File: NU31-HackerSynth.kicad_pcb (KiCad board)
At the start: 2 copper layers, 180 x 110 mm, 137 parts, among them J1 Conn_02x09_Odd_Even, J2 GREEN, J3 Barrel_Jack, J4 AudioJack2_SwitchT, J5 AudioJack2_SwitchT, J6 AudioJack2_SwitchT, J7 Eurorack Power, Q1 BC547, Q2 BC547, Q3 BC547, Q4 BC547, SW1 SW_DPDT, SW2 SW_SPDT, SW3 SW_Rotary_1x8_MP, U1 LM358, U2 LM358, U3 LM358, U4 CD4017, U5 LM358, U6 LM358, U7 LM358

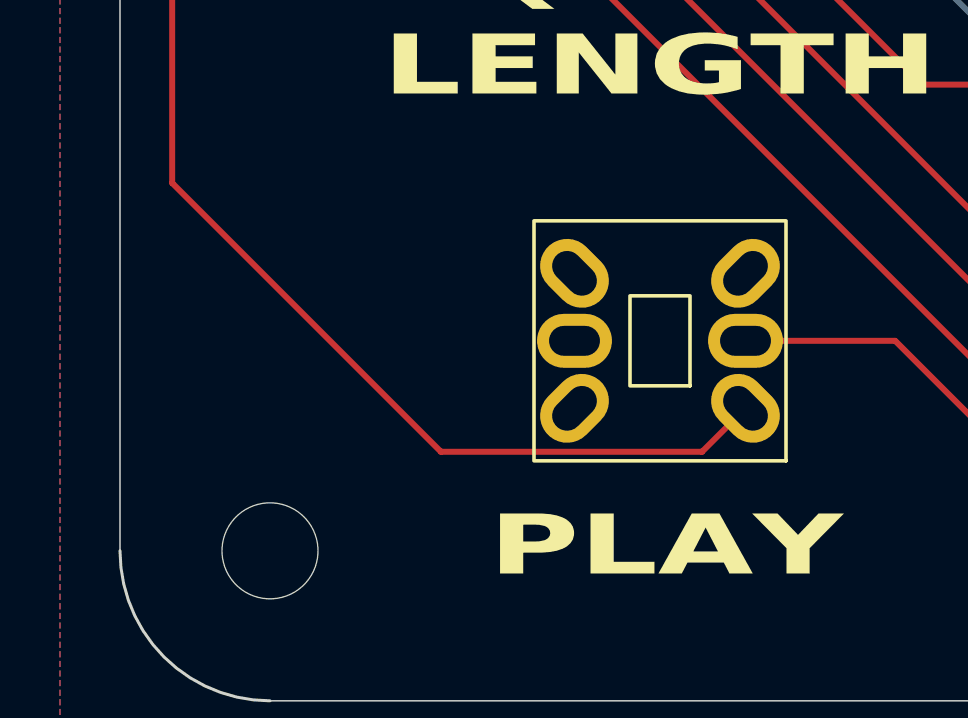
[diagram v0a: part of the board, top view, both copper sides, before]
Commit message: fixed clock switch pinout and footprint
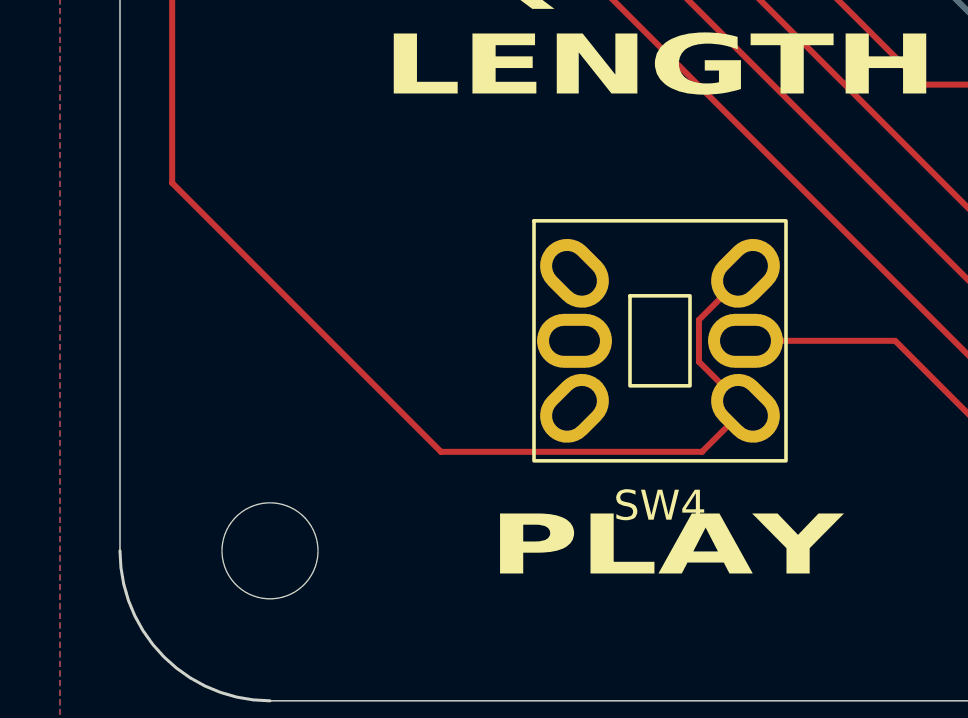
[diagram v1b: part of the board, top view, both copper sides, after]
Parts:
- removed SW2: SW_SPDT, SpaceCow:8x8_DPDT_Push_Button
- added SW4: SW_DPST, SpaceCow:8x8_DPDT_Push_Button, F.Cu at (68.0, 148.0)
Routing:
- net /SEQ_CLOCK_IN: track 223.2 -> 229.0 mm
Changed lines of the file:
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@@
 		)
 	)
+	(footprint "SpaceCow:8x8_DPDT_Push_Button"
+		(layer "F.Cu")
+		(at 68 148)
+		(property "Reference" "SW4"
+			(at 0 5.5 0)
+			(unlocked yes)
+			(layer "F.SilkS")
+			(effects
+				(font
+					(size 1 1)
+					(thickness 0.15)
+				)
+			)
+		)
+		(property "Value" "SW_DPST"
+			(at 0 7 0)
+			(unlocked yes)
+			(layer "F.Fab")
+			(effects
+				(font
+					(size 1 1)
+					(thickness 0.15)
+				)
+			)
+		)
+		(property "Datasheet" "~"
+			(at 0 0 0)
+			(unlocked yes)
+			(layer "F.Fab")
+			(hide yes)
+			(effects
+				(font
+					(size 1 1)
+					(thickness 0.15)
+				)
+			)
+		)
+		(property "Description" "Double Pole Single Throw (DPST) Switch"
+			(at 0 0 0)
+			(unlocked yes)
+			(layer "F.Fab")
+			(hide yes)
+			(effects
+				(font
+					(size 1 1)
+					(thickness 0.15)
+				)
+			)
+		)
+		(sheetname "/")
+		(sheetfile "NU31-HackerSynth.kicad_sch")
+		(attr through_hole)
+		(fp_rect
+			(start -4.2 -4)
+			(end 4.2 4)
+			(stroke
+				(width 0.12)
+				(type default)
+			)
+			(fill no)
+			(layer "F.SilkS")
+		)
+		(fp_rect
+			(start -1 -1.5)
+			(end 1 1.5)
+			(stroke
+				(width 0.12)
+				(type default)
+			)
+			(fill no)
+			(layer "F.SilkS")
+		)
+		(fp_rect
+			(start -4.4 -4.2)
+			(end 4.4 4.2)
+			(stroke
+				(width 0.05)
+				(type default)
+			)
+			(fill no)
+			(layer "F.CrtYd")
+		)
+		(fp_text user "${REFERENCE}"
+			(at -0.2 9.1 0)
+			(unlocked yes)
+			(layer "F.Fab")
+			(effects
+				(font
+					(size 1 1)
+					(thickness 0.15)
+				)
+			)
+		)
+		(pad "1" thru_hole oval
+			(at -2.85 -2.25 315)
+			(size 2.5 1.8)
+			(drill oval 1.7 1)
+			(layers "*.Cu" "*.Mask")
+			(remove_unused_layers no)
+			(net 1 "GND")
+			(pinfunction "1")
+			(pintype "passive")
+		)
+		(pad "1" thru_hole oval
+			(at -2.85 2.25 225)
+			(size 2.5 1.8)
+			(drill oval 1.7 1)
+			(layers "*.Cu" "*.Mask")
+			(remove_unused_layers no)
+			(net 1 "GND")
+			(pinfunction "1")
+			(pintype "passive")
+		)
+		(pad "2" thru_hole oval
+			(at -2.85 0 180)
+			(size 2.5 1.8)
+			(drill oval 1.7 1)
+			(layers "*.Cu" "*.Mask")
+			(remove_unused_layers no)
+			(net 1 "GND")
+			(pinfunction "2")
+			(pintype "passive")
+		)
+		(pad "3" thru_hole oval
+			(at 2.85 -2.25 225)
+			(size 2.5 1.8)
+			(drill oval 1.7 1)
+			(layers "*.Cu" "*.Mask")
+			(remove_unused_layers no)
+			(net 45 "/SEQ_CLOCK_IN")
+			(pinfunction "3")
+			(pintype "passive")
+		)
+		(pad "3" thru_hole oval
+			(at 2.85 2.25 135)
+			(size 2.5 1.8)
+			(drill oval 1.7 1)
+			(layers "*.Cu" "*.Mask")
+			(remove_unused_layers no)
+			(net 45 "/SEQ_CLOCK_IN")
+			(pinfunction "3")
+			(pintype "passive")
+		)
+		(pad "4" thru_hole oval
+			(at 2.85 0 180)
+			(size 2.5 1.8)
+			(drill oval 1.7 1)
+			(layers "*.Cu" "*.Mask")
+			(remove_unused_layers no)
+			(net 99 "Net-(R59-Pad2)")
+			(pinfunction "4")
+			(pintype "passive")
+		)
+		(embedded_fonts no)
+	)
 	(footprint "Resistor_THT:R_Axial_DIN0207_L6.3mm_D2.5mm_P10.16mm_Horizontal"
 		(layer "F.Cu")
@@
 		(embedded_fonts no)
 	)
-	(footprint "SpaceCow:8x8_DPDT_Push_Button"
-		(locked yes)
-		(layer "F.Cu")
-		(at 68 148 180)
-		(property "Reference" "SW2"
-			(at 0 -3 180)
-			(unlocked yes)
-			(layer "F.SilkS")
-			(hide yes)
-			(effects
-				(font
-					(size 0.8 0.8)
-					(thickness 0.16)
-					(bold yes)
-				)
-			)
-		)
-		(property "Value" "SW_SPDT"
-			(at 0 0 180)
-			(unlocked yes)
-			(layer "F.SilkS")
-			(hide yes)
-			(effects
-				(font
-					(size 0.8 0.65)
-					(thickness 0.15)
-					(italic yes)
-				)
-			)
-		)
-		(property "Datasheet" "~"
-			(at 0 0 180)
-			(unlocked yes)
-			(layer "F.Fab")
-			(hide yes)
-			(effects
-				(font
-					(size 1 1)
-					(thickness 0.15)
-				)
-			)
-		)
-		(property "Description" "Slide Switch, dual pole double throw"
-			(at 0 0 180)
-			(unlocked yes)
-			(layer "F.Fab")
-			(hide yes)
-			(effects
-				(font
-					(size 1 1)
-					(thickness 0.15)
-				)
-			)
-		)
-		(sheetname "/")
-		(sheetfile "NU31-HackerSynth.kicad_sch")
-		(attr through_hole)
-		(fp_rect
-			(start -1 -1.5)
-			(end 1 1.5)
-			(stroke
-				(width 0.12)
-				(type default)
-			)
-			(fill no)
-			(layer "F.SilkS")
-		)
-		(fp_rect
-			(start -4.2 -4)
-			(end 4.2 4)
-			(stroke
-				(width 0.12)
-				(type default)
-			)
-			(fill no)
-			(layer "F.SilkS")
-		)
-		(fp_rect
-			(start -4.4 -4.2)
-			(end 4.4 4.2)
-			(stroke
-				(width 0.05)
-				(type default)
-			)
-			(fill no)
-			(layer "F.CrtYd")
-		)
-		(fp_text user "${REFERENCE}"
-			(at -0.2 9.1 180)
-			(unlocked yes)
-			(layer "F.Fab")
-			(effects
-				(font
-					(size 0.8 0.8)
-					(thickness 0.16)
-					(bold yes)
-				)
-			)
-		)
-		(pad "1" thru_hole oval
-			(at -2.85 -2.25 135)
-			(size 2.5 1.8)
-			(drill oval 1.7 1)
-			(layers "*.Cu" "*.Mask")
-			(remove_unused_layers no)
-			(net 45 "/SEQ_CLOCK_IN")
-			(pinfunction "A")
-			(pintype "passive")
-		)
-		(pad "2" thru_hole oval
-			(at -2.85 0)
-			(size 2.5 1.8)
-			(drill oval 1.7 1)
-			(layers "*.Cu" "*.Mask")
-			(remove_unused_layers no)
-			(net 99 "Net-(R59-Pad2)")
-			(pinfunction "B")
-			(pintype "passive")
-		)
-		(pad "3" thru_hole oval
-			(at -2.85 2.25 45)
-			(size 2.5 1.8)
-			(drill oval 1.7 1)
-			(layers "*.Cu" "*.Mask")
-			(remove_unused_layers no)
-			(net 1 "GND")
-			(pinfunction "C")
-			(pintype "passive")
-		)
-		(pad "4" thru_hole oval
-			(at 2.85 -2.25 45)
-			(size 2.5 1.8)
-			(drill oval 1.7 1)
-			(layers "*.Cu" "*.Mask")
-			(remove_unused_layers no)
-			(net 1 "GND")
-			(pinfunction "A")
-			(pintype "passive")
-		)
-		(pad "5" thru_hole oval
-			(at 2.85 0)
-			(size 2.5 1.8)
-			(drill oval 1.7 1)
-			(layers "*.Cu" "*.Mask")
-			(remove_unused_layers no)
-			(net 1 "GND")
-			(pinfunction "B")
-			(pintype "passive")
-		)
-		(pad "6" thru_hole oval
-			(at 2.85 2.25 315)
-			(size 2.5 1.8)
-			(drill oval 1.7 1)
-			(layers "*.Cu" "*.Mask")
-			(remove_unused_layers no)
-			(net 1 "GND")
-			(pinfunction "C")
-			(pintype "passive")
-		)
-		(embedded_fonts no)
-	)
 	(footprint "Capacitor_THT:C_Disc_D5.1mm_W3.2mm_P5.00mm"
 		(layer "F.Cu")
@@
 	)
 	(segment
-		(start 148.64026 53)
-		(end 151.3 55.65974)
+		(start 69.299 147.301)
+		(end 69.299 148.699)
 		(width 0.2)
 		(layer "F.Cu")
@@
 	)
 	(segment
-		(start 60.698486 151.698486)
-		(end 51.739 142.739)
+		(start 151.3 71.4925)
+		(end 149.5125 73.28)
 		(width 0.2)
 		(layer "F.Cu")
@@
 	)
 	(segment
-		(start 69.401514 151.698486)
-		(end 60.698486 151.698486)
+		(start 60.7 151.7)
+		(end 51.739 142.739)
 		(width 0.2)
 		(layer "F.Cu")
@@
 	)
 	(segment
-		(start 151.3 55.65974)
-		(end 151.3 71.4925)
+		(start 148.64026 53)
+		(end 151.3 55.65974)
 		(width 0.2)
 		(layer "F.Cu")
@@
 	)
 	(segment
-		(start 151.3 71.4925)
-		(end 149.5125 73.28)
+		(start 69.4 151.7)
+		(end 60.7 151.7)
 		(width 0.2)
 		(layer "F.Cu")
@@
 	)
 	(segment
-		(start 51.739 142.739)
-		(end 51.739 68.361)
+		(start 69.299 148.699)
+		(end 70.85 150.25)
 		(width 0.2)
 		(layer "F.Cu")
@@
 	)
 	(segment
+		(start 51.739 142.739)
+		(end 51.739 68.361)
+		(width 0.2)
+		(layer "F.Cu")
+		(net 45)
+	)
+	(segment
+		(start 70.85 145.75)
+		(end 69.299 147.301)
+		(width 0.2)
+		(layer "F.Cu")
+		(net 45)
+	)
+	(segment
+		(start 151.3 55.65974)
+		(end 151.3 71.4925)
+		(width 0.2)
+		(layer "F.Cu")
+		(net 45)
+	)
+	(segment
 		(start 70.85 150.25)
-		(end 69.401514 151.698486)
+		(end 69.4 151.7)
 		(width 0.2)
 		(layer "F.Cu")

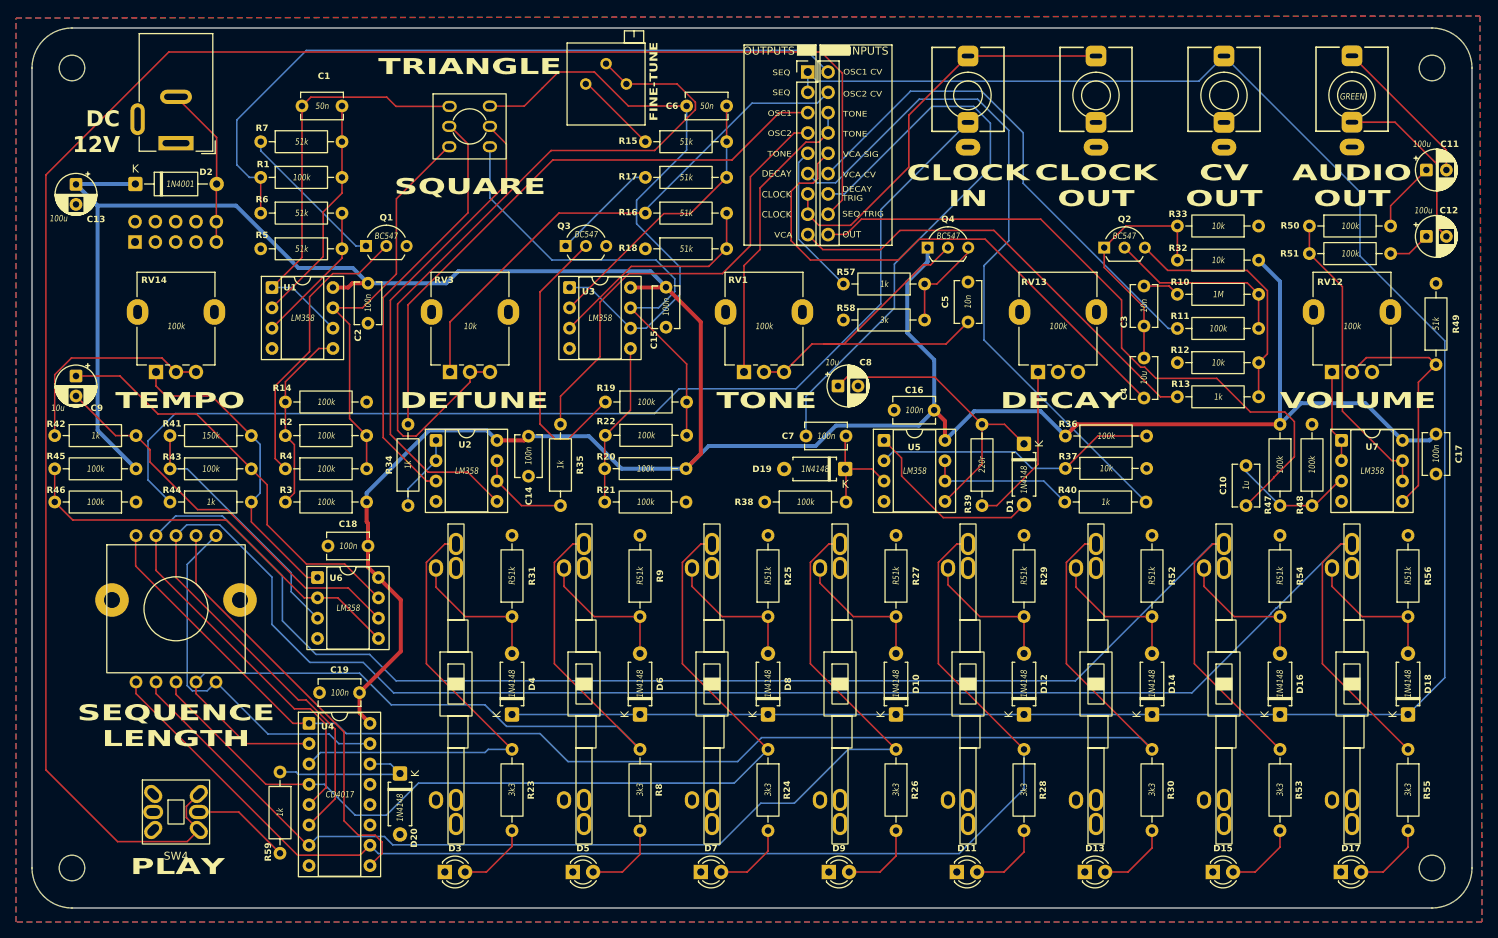
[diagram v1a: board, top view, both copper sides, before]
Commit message: updated fader footprint, fixed DC barrel polarity in the layout
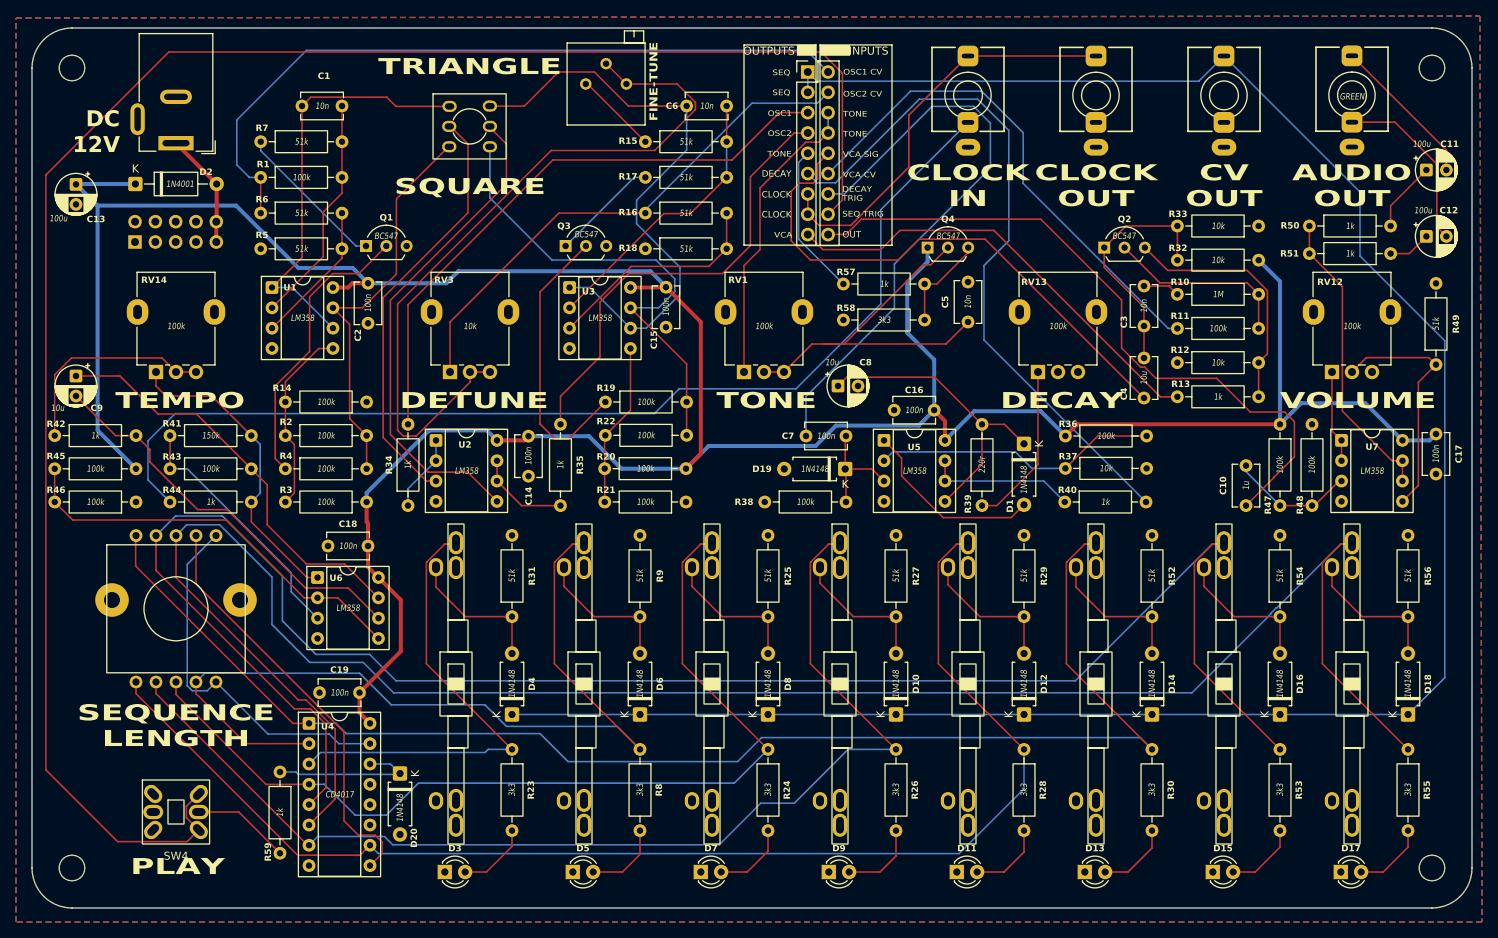
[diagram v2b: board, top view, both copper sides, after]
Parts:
- C1, C6: value 50n -> 10n
- R25, R27, R29, R31, R52, R54, R56, R9: value R51k -> 51k
- R50, R51: value 100k -> 1k
- R58: value 3k -> 3k3
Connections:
- J3 pad 1: GND -> Net-(D2-A)
- J3 pad 2: Net-(D2-A) -> GND
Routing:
- net Net-(D2-A): track 20.3 -> 14.6 mm
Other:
- board text added: "Kosmichna KOROVA"
- board text added: "PROTOTYPE 2 (NOV 2025)"
